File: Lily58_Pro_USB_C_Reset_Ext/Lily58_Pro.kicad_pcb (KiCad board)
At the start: 2 copper layers, 142.5 x 106.3 mm, 87 parts, among them J1 LED, J2 4PIN, J3 OLED, P1 i2c_pin, P2 i2c_pin, SW1 SW_PUSH, SW10 SW_PUSH, SW11 SW_PUSH, SW12 SW_PUSH, SW13 SW_PUSH, SW14 SW_PUSH, SW15 SW_PUSH, SW16 SW_PUSH, SW17 SW_PUSH, SW18 SW_PUSH, SW19 SW_PUSH, SW2 SW_PUSH, SW20 SW_PUSH, SW21 SW_PUSH, SW22 SW_PUSH, SW23 SW_PUSH, SW24 SW_PUSH, SW25 SW_PUSH, SW26 SW_PUSH, SW27 SW_PUSH, SW28 SW_PUSH, SW29 SW_PUSH, SW3 SW_PUSH, SW4 SW_PUSH, SW5 SW_PUSH, SW6 SW_PUSH, SW7 SW_PUSH, SW8 SW_PUSH, SW9 SW_PUSH, U1 ProMicro

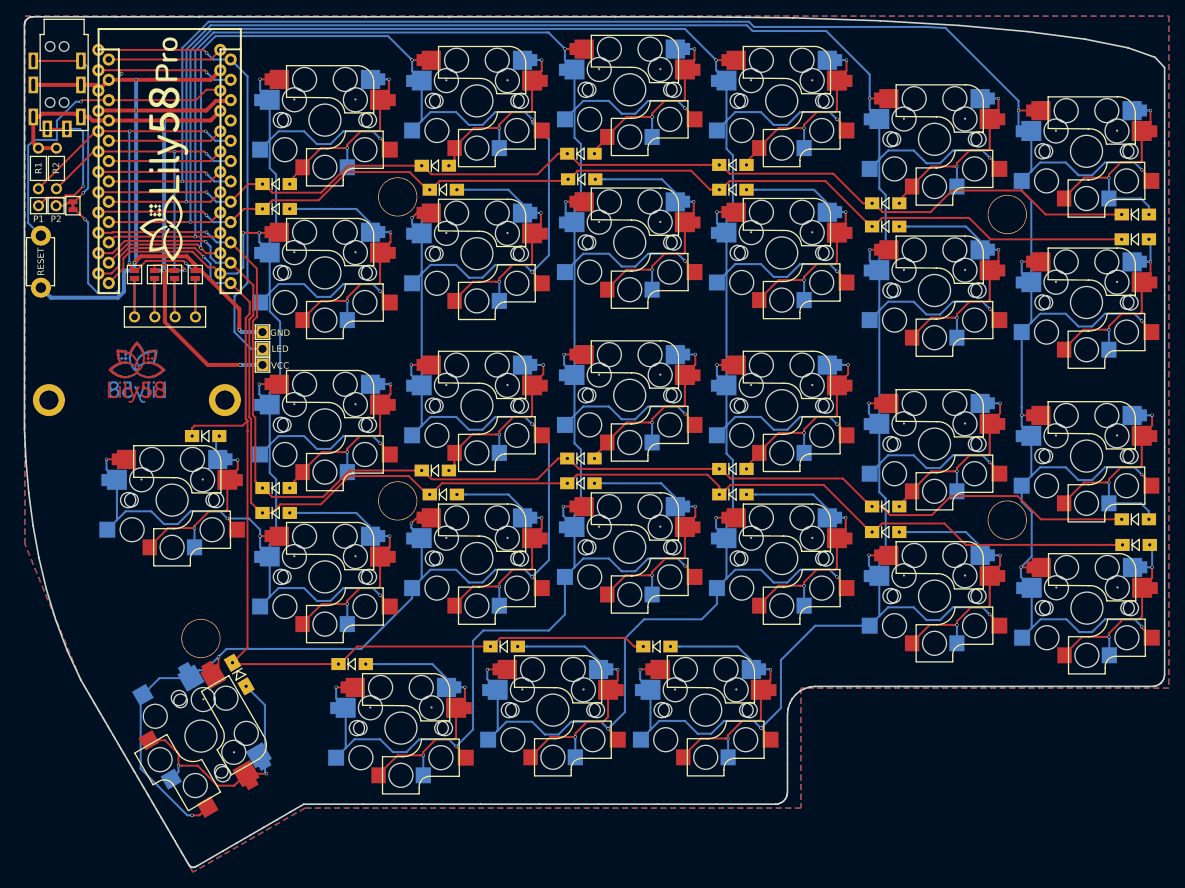
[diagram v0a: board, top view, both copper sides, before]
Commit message: Lily58_Pro_USB_C_Reset_Ext: convert to new KiCad format
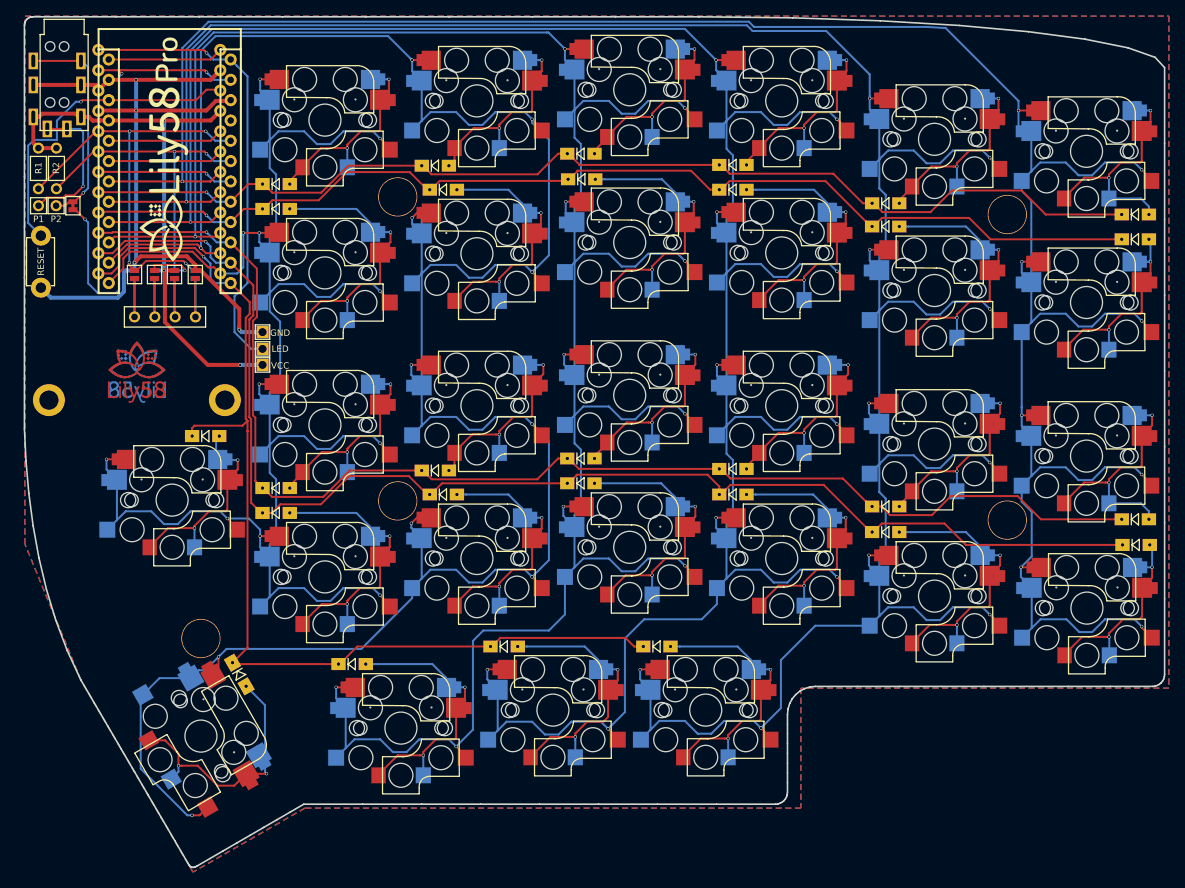
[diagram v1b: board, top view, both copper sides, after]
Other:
- net class Default removed
- net class GND removed
- net class VCC removed

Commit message: Lily58_Pro_USB_C_Reset_Ext: strip down
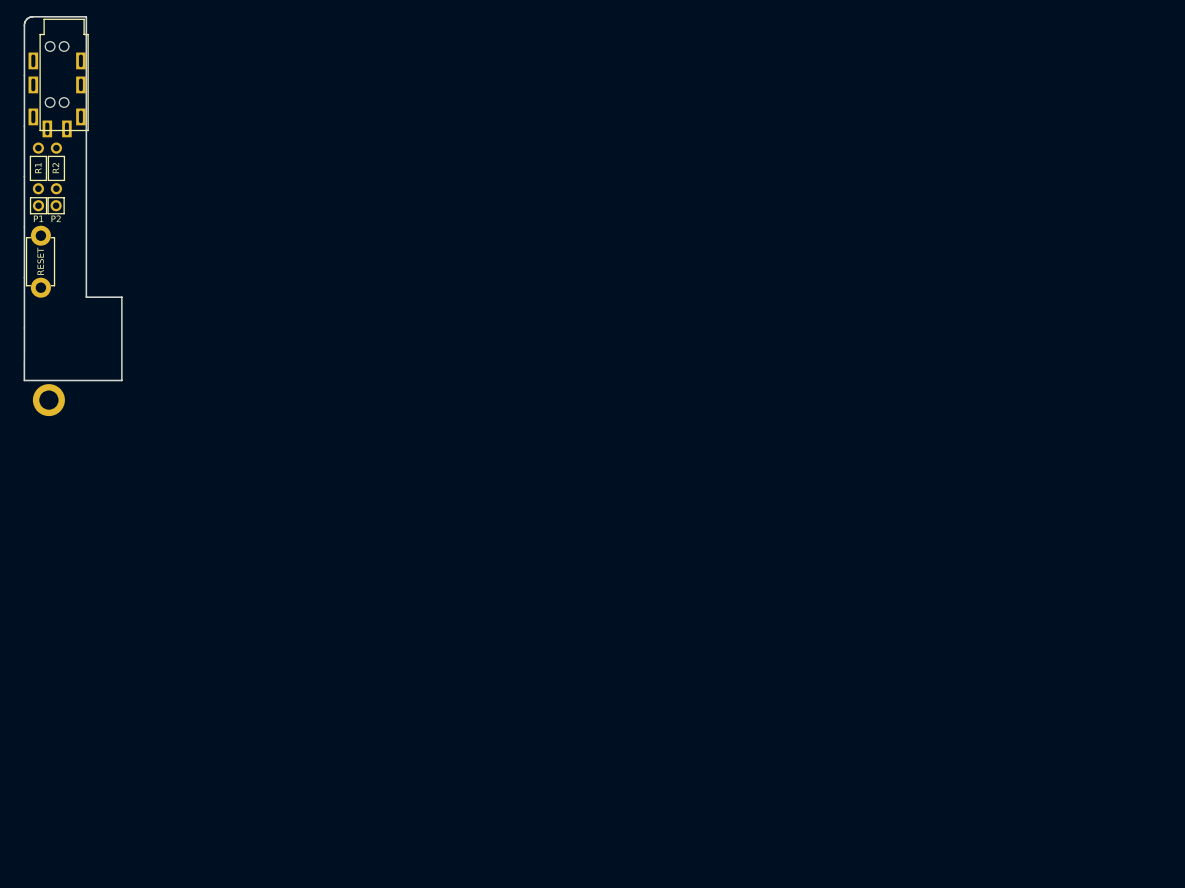
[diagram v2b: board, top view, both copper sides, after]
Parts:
- removed D1, D10, D11, D12, D13, D14, D15, D16, D17, D18, D19, D2, D20, D21, D22, D23, D24, D25, D26, D27, D28, D29, D3, D4, D5, D6, D7, D8, D9: D, Lily58-footprint:Diode_SOD123
- removed G*** (x2): LOGO, Lily58-footprint:lily58_logo_Pro
- removed G*** (x2): LOGO, Lily58-footprint:lily58_logo_2
- removed J1: LED, Lily58-footprint:LED
- removed J3: OLED, Lily58-footprint:OLED_4Pin
- removed JP1, JP2, JP3, JP4, JP5, JP6, JP7, JP8: , Lily58-footprint:Jumper
- removed SW1, SW10, SW11, SW12, SW13, SW14, SW15, SW16, SW17, SW18, SW19, SW2, SW20, SW21, SW22, SW23, SW24, SW25, SW26, SW27, SW28, SW29, SW3, SW4, SW5, SW6, SW7, SW8, SW9: SW_PUSH, Lily58-footprint:CherryMX_KailhLowProfile_Hotswap_edge
- removed TH2: HOLE, Lily58-footprint:M2_HOLE_PCB
- removed TH3, TH4, TH5, TH6, TH7: HOLE, Lily58-footprint:HOLE_M2_TH
- removed U1: ProMicro, Lily58-footprint:ProMicro_rev2
- removed W1: jumper, Lily58-footprint:jumper_data
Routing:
- net col1: track 350.6 -> 0.00 mm, vias 11 -> 0
- net col2: track 334.4 -> 0.00 mm, vias 11 -> 0
- net col3: track 319.9 -> 0.00 mm, vias 11 -> 0
- net col4: track 319.5 -> 0.00 mm, vias 11 -> 0
- net col0: track 304.4 -> 0.00 mm, vias 9 -> 0
- net col5: track 235.9 -> 0.00 mm, vias 11 -> 0
- net row3: track 170.1 -> 0.00 mm, vias 1 -> 0
- net row2: track 165.8 -> 0.00 mm, vias 1 -> 0
- net row1: track 138.3 -> 0.00 mm, vias 1 -> 0
- net row0: track 138.2 -> 0.00 mm, vias 1 -> 0
- net row4: track 132.6 -> 0.00 mm, vias 1 -> 0
- net GND: track 103.0 -> 0.00 mm, vias 4 -> 0
- net VCC: track 72.9 -> 0.00 mm, vias 3 -> 0
- net DATA: track 59.7 -> 0.00 mm, vias 3 -> 0
- net LED: track 57.0 -> 0.00 mm, vias 1 -> 0
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- removed copper zone on B.Cu, net GND
- removed copper zone on F.Cu, net GND
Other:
- board size 142.5 x 106.3 mm -> 12.2 x 45.5 mm

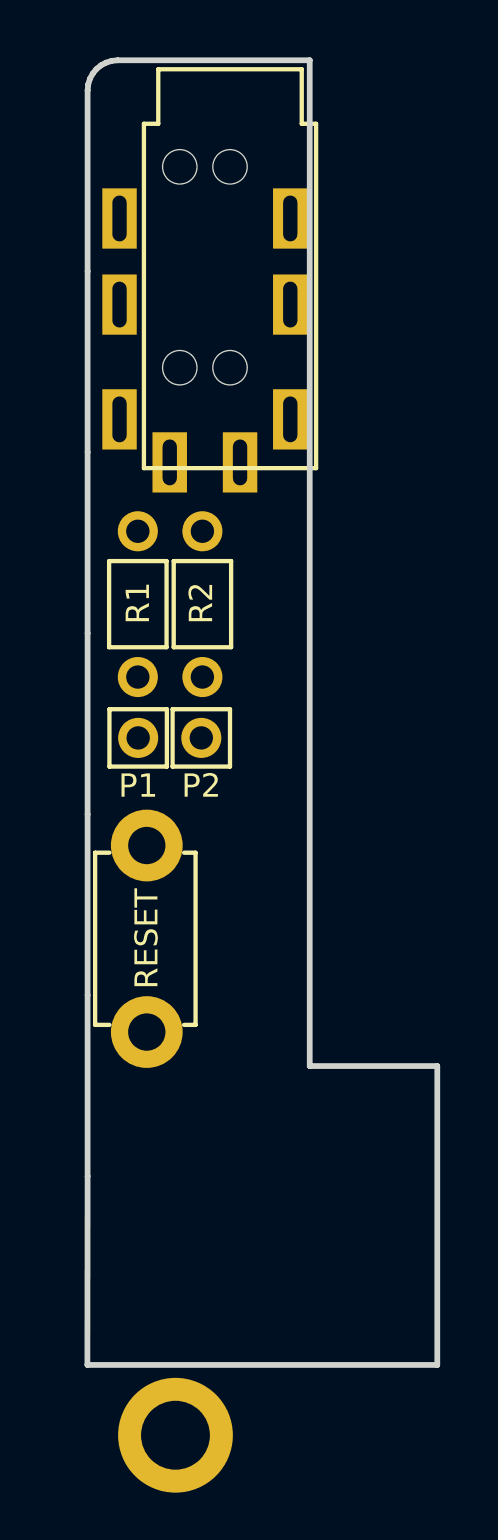
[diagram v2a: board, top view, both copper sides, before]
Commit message: Lily58_Pro_USB_C_Reset_Ext: add usb and reset
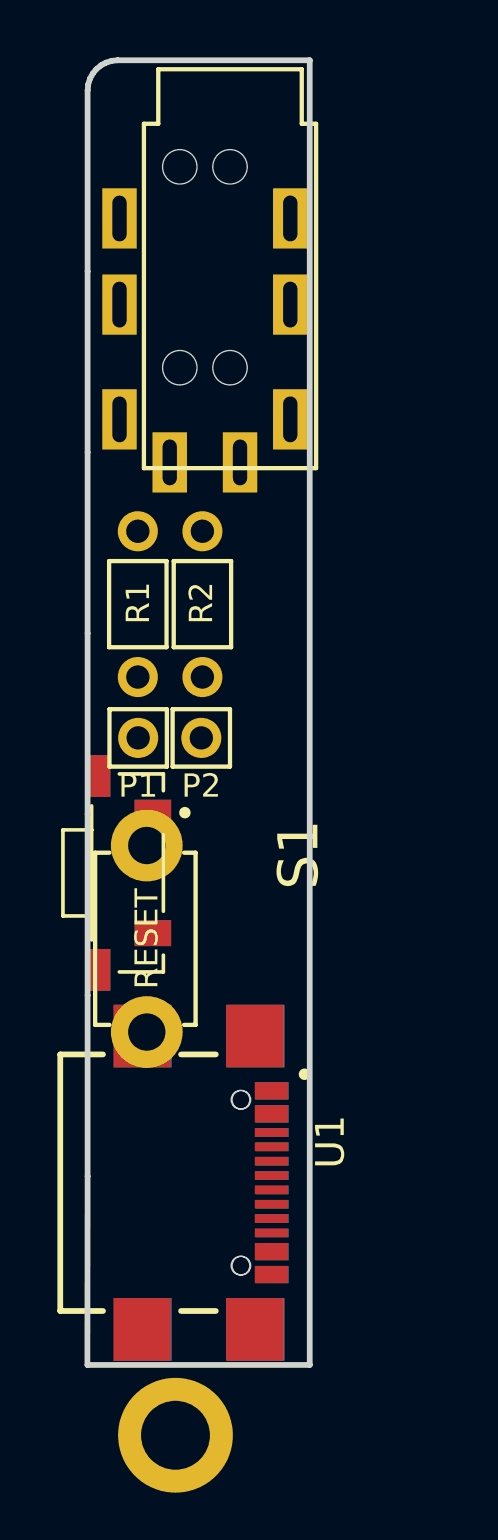
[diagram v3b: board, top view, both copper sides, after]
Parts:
- added S1: TL3330AF130QG, TL3330AF130QG:SW_TL3330AF130QG, F.Cu at (84.3, 65.4)
- added S2: TL3330AF130QG, TL3330AF130QG:SW_TL3330AF130QG, B.Cu at (84.3, 65.4)
- added U1: USB4110-GF-A_REVB, Usb:GCT_USB4110-GF-A_REVB, F.Cu at (88.3, 76.2)
- added U2: USB4110-GF-A_REVB, Usb:GCT_USB4110-GF-A_REVB, B.Cu at (88.3, 76.2)
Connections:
- J2 pad 3: Net-(J2-Pad3) -> SCL
- J2 pad 4: Net-(J2-Pad4) -> SDA
- P1 pad 1: Net-(J2-Pad4) -> unconnected-(P1-Pad1)
- P2 pad 1: Net-(J2-Pad3) -> unconnected-(P2-Pad1)
- R1 pad 1: VCC -> unconnected-(R1-Pad1)
- R1 pad 2: SDA -> unconnected-(R1-Pad2)
- R2 pad 1: VCC -> unconnected-(R2-Pad1)
- R2 pad 2: SCL -> unconnected-(R2-Pad2)
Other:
- board size 12.2 x 45.5 mm -> 7.7 x 45.5 mm
